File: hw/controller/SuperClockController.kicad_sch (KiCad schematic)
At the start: 64 parts, among them J1 USB_A, J2 ATmega ISP, J3 Led Cathodes, J4 Led Anodes, J5 Yellow LED 0, J6 Yellow LED 1, Q1 IRLML2502, Q10 IRLML2502, Q11 IRLML2502, Q12 IRLML2502, Q13 IRLML2502, Q14 IRLML2502, Q15 IRLML2502, Q16 IRLML2502, Q17 IRLML2502, Q18 IRLML2502, Q2 IRLML2502, Q3 IRLML2502, Q4 IRLML2502, Q5 IRLML2502, Q6 IRLML2502, Q7 IRLML2502, Q8 IRLML2502, Q9 IRLML2502, SW1 SW_Push, SW2 SW_Push, SW3 SW_Push, U1 ATmega32A-A, U2 DS3231SN, U3 DS1307ZN, Y1 16MHz, Y2 32.768kHz

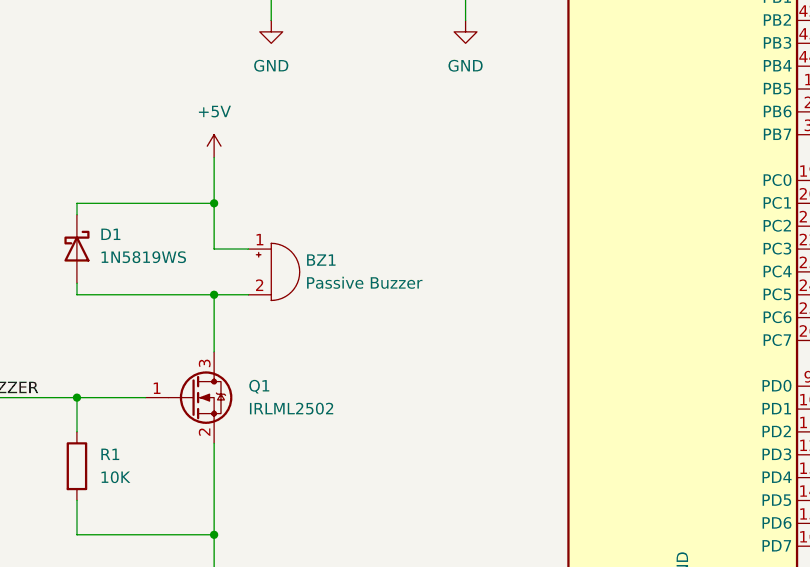
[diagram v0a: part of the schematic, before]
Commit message: Mention buzzer resistance on schematic
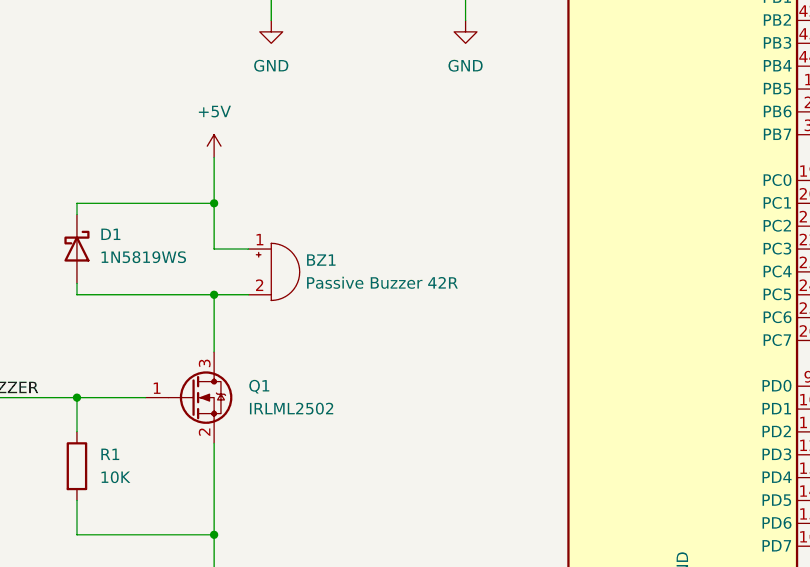
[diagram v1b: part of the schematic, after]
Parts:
- BZ1: value Passive Buzzer -> Passive Buzzer 42R
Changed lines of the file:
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@@
 			)
 		)
-		(property "Value" "Passive Buzzer"
+		(property "Value" "Passive Buzzer 42R"
 			(at 62.23 152.3999 0)
 			(effects

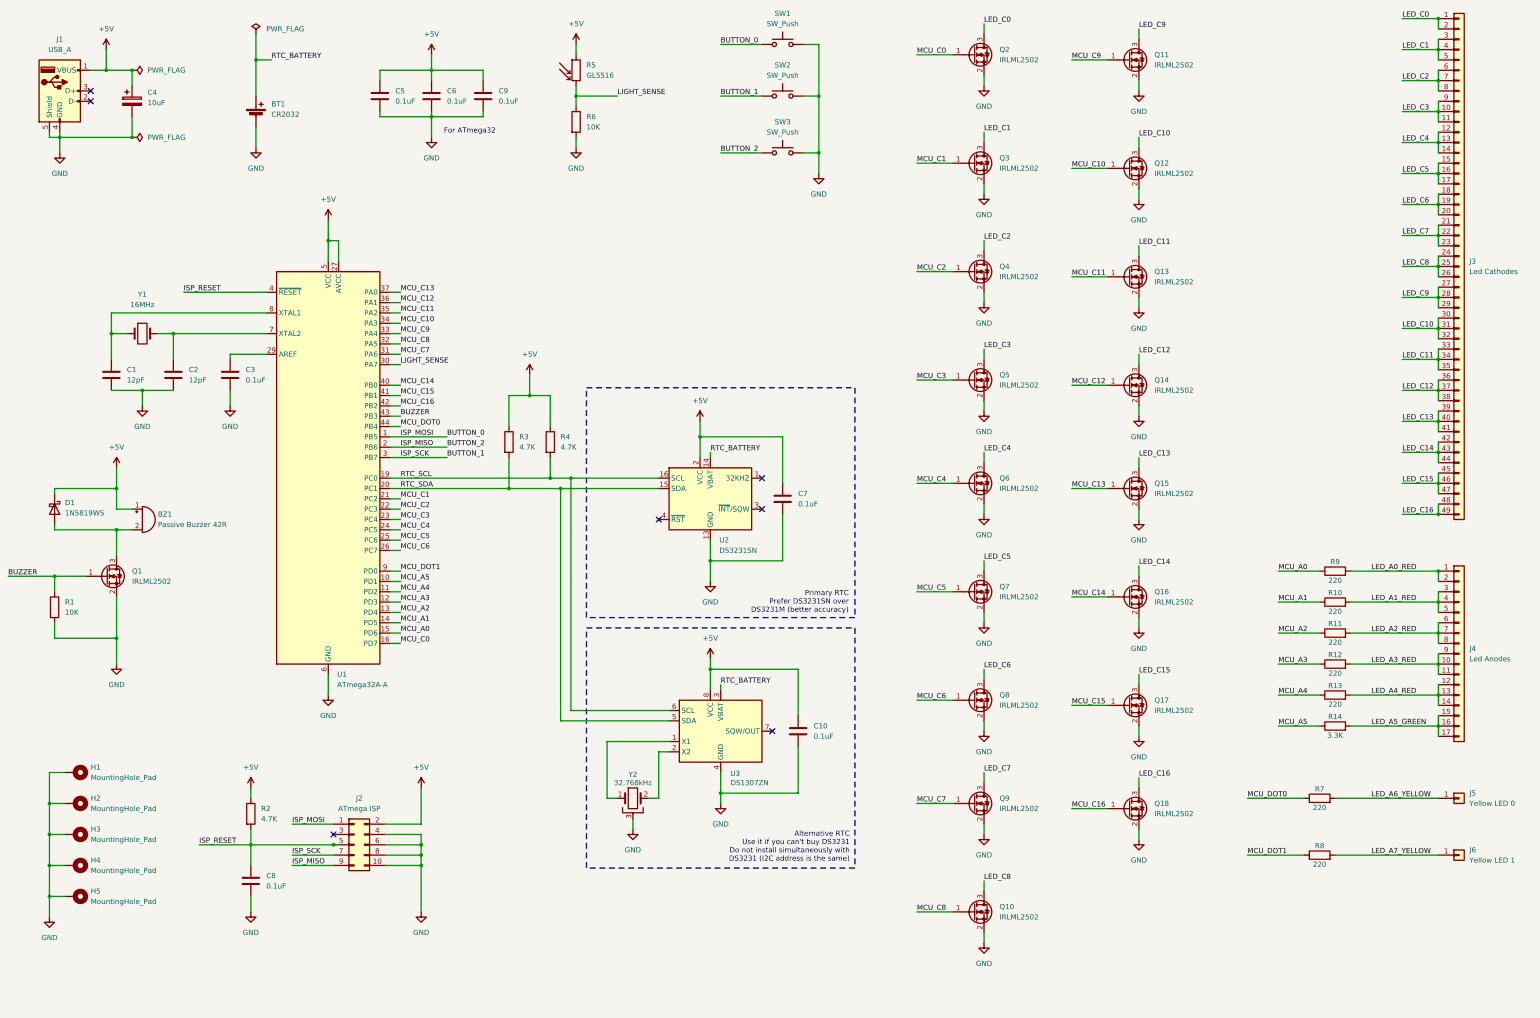
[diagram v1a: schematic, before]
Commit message: Controller PCB revision 3.1
- Add cathode pull-ups. It seems to be the only proper way to deal with ghosting and flickering on lowest brightness
- Connect all anodes to one MCU port, should provide more opportunities to software.
- Use smaller silk-screen outline for CR2032 holder (the previous one was visibly offset for my battery holder).
- Update component numbering with a more sensible scheme: cathode FETs and resistors are now numbers 1-17.
- Use bigger footprint and bigger value for power input capacitor.
- Add missing capacitor to one of MCU power pins.
- Move crystal closer to MCU.
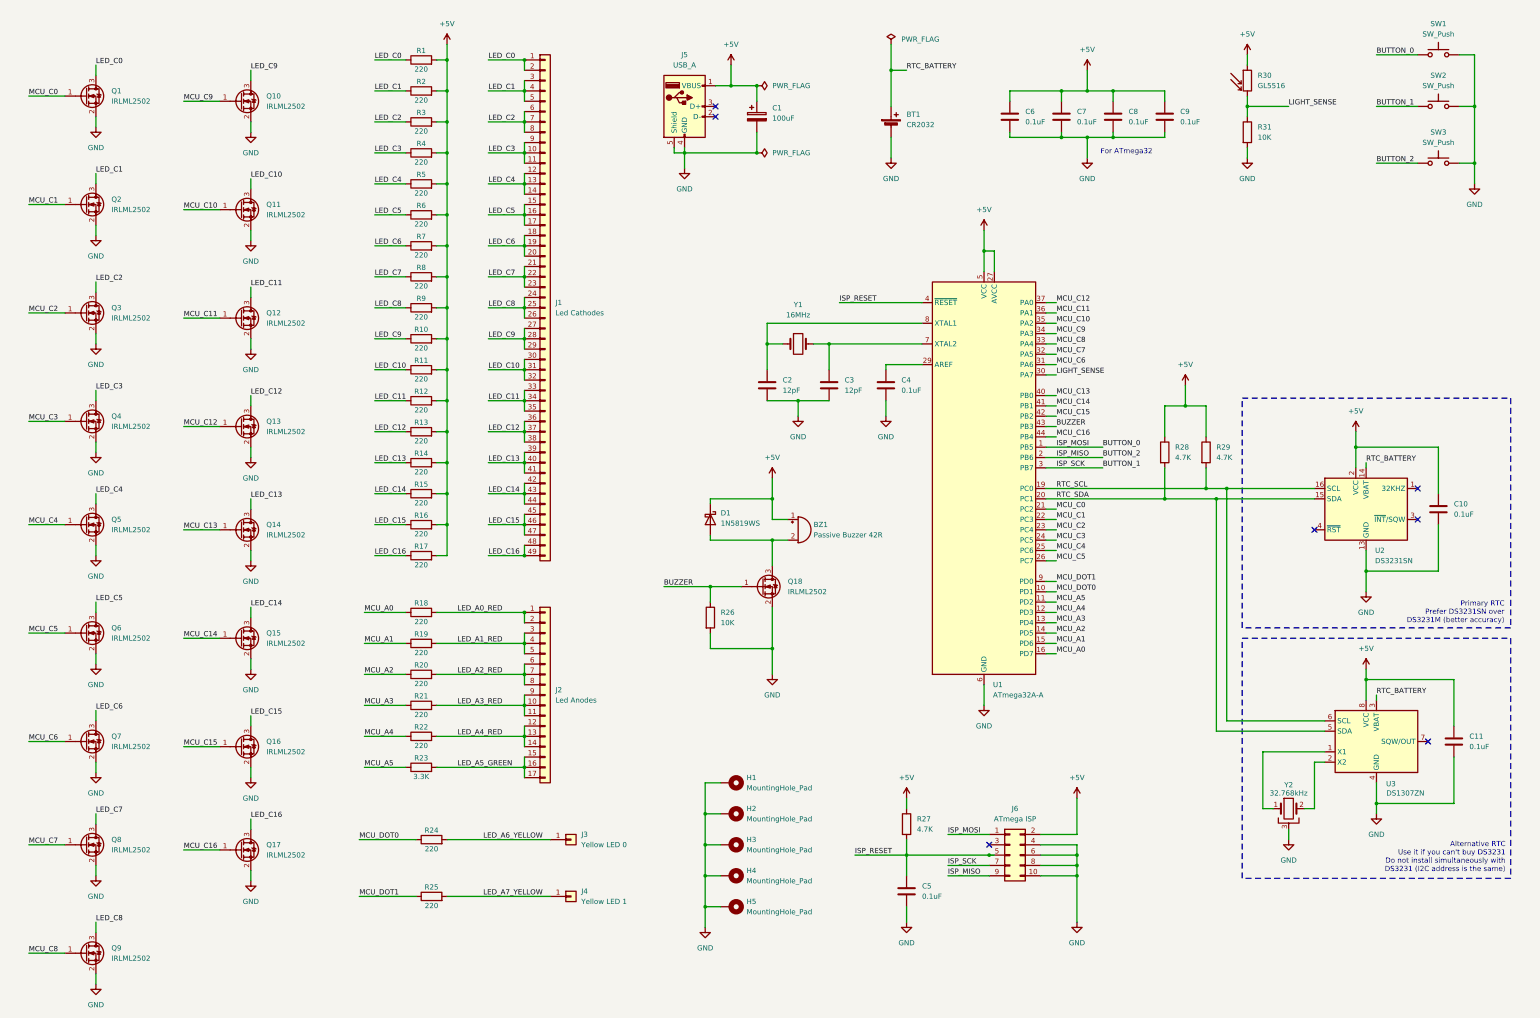
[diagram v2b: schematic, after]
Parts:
- added C9: 0.1uF, Capacitor_SMD:C_0805_2012Metric_Pad1.18x1.45mm_HandSolder, symbol Device:C
- added R1, R10, R11, R12, R13, R14, R15, R16, R17, R2, R3, R4, R5, R6, R7, R8, R9: 220, Resistor_SMD:R_0805_2012Metric_Pad1.20x1.40mm_HandSolder, symbol Device:R
- BT1: footprint Battery:Battery_Panasonic_CR2032-HFN_Horizontal_CircularHoles -> @Project:Battery_CR2032
- BZ1: footprint @Project:Buzzer_12x7.5RM6.5 -> @Project:Buzzer_12x8.5
- C1: renamed from C4; value 10uF -> 100uF; footprint Capacitor_Tantalum_SMD:CP_EIA-6032-28_Kemet-C_Pad2.25x2.35mm_HandSolder -> Capacitor_Tantalum_SMD:CP_EIA-7343-31_Kemet-D_Pad2.25x2.55mm_HandSolder
- renumbered C7 to C10, C10 to C11, C1 to C2, C2 to C3, C3 to C4, C8 to C5, C5 to C6, C6 to C7, C9 to C8, J3 to J1, J4 to J2, J5 to J3, J6 to J4, J1 to J5, J2 to J6, Q2 to Q1, Q11 to Q10, Q12 to Q11, Q13 to Q12, Q14 to Q13, Q15 to Q14, Q16 to Q15, Q17 to Q16, Q18 to Q17, Q1 to Q18, Q3 to Q2, Q4 to Q3, Q5 to Q4, Q6 to Q5, Q7 to Q6, Q8 to Q7, Q9 to Q8, Q10 to Q9, R9 to R18, R10 to R19, R11 to R20, R12 to R21, R13 to R22, R14 to R23, R7 to R24, R8 to R25, R1 to R26, R2 to R27, R3 to R28, R4 to R29, R5 to R30, R6 to R31
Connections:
- net +5V: now also C9.1, R1.2, R10.2, R11.2, R12.2, R13.2, R14.2, R15.2, R16.2, R17.2, R2.2, R3.2, R4.2, R5.2, R6.2, R7.2, R8.2, R9.2
- net GND: now also C9.2
- net LED_C0: now also R1.1
- net LED_C1: now also R2.1
- net LED_C10: now also R11.1
- net LED_C11: now also R12.1
- net LED_C12: now also R13.1
- net LED_C13: now also R14.1
- net LED_C14: now also R15.1
- net LED_C15: now also R16.1
- net LED_C16: now also R17.1
- net LED_C2: now also R3.1
- net LED_C3: now also R4.1
- net LED_C4: now also R5.1
- net LED_C5: now also R6.1
- net LED_C6: now also R7.1
- net LED_C7: now also R8.1
- net LED_C8: now also R9.1
- net LED_C9: now also R10.1
- net MCU_A0: now also U1.16 (PD7); no longer U1.15 (PD6)
- net MCU_A1: now also U1.15 (PD6); no longer U1.14 (PD5)
- net MCU_A2: now also U1.14 (PD5); no longer U1.13 (PD4)
- net MCU_A3: now also U1.13 (PD4); no longer U1.12 (PD3)
- net MCU_A4: now also U1.12 (PD3); no longer U1.11 (PD2)
- net MCU_A5: now also U1.11 (PD2); no longer U1.10 (PD1)
- net MCU_C0: now also U1.21 (PC2); no longer U1.16 (PD7)
- net MCU_C1: now also U1.22 (PC3); no longer U1.21 (PC2)
- net MCU_C10: now also U1.35 (PA2); no longer U1.34 (PA3)
- net MCU_C11: now also U1.36 (PA1); no longer U1.35 (PA2)
- net MCU_C12: now also U1.37 (PA0); no longer U1.36 (PA1)
- net MCU_C13: now also U1.40 (PB0); no longer U1.37 (PA0)
- net MCU_C14: now also U1.41 (PB1); no longer U1.40 (PB0)
- net MCU_C15: now also U1.42 (PB2); no longer U1.41 (PB1)
- net MCU_C16: now also U1.44 (PB4); no longer U1.42 (PB2)
- net MCU_C2: now also U1.23 (PC4); no longer U1.22 (PC3)
- net MCU_C3: now also U1.24 (PC5); no longer U1.23 (PC4)
- net MCU_C4: now also U1.25 (PC6); no longer U1.24 (PC5)
- net MCU_C5: now also U1.26 (PC7); no longer U1.25 (PC6)
- net MCU_C6: now also U1.31 (PA6); no longer U1.26 (PC7)
- net MCU_C7: now also U1.32 (PA5); no longer U1.31 (PA6)
- net MCU_C8: now also U1.33 (PA4); no longer U1.32 (PA5)
- net MCU_C9: now also U1.34 (PA3); no longer U1.33 (PA4)
- net MCU_DOT0: now also U1.10 (PD1); no longer U1.44 (PB4)
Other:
- title: SuperClock v3 Controller -> SuperClock v3.1 Controller
- moved on the sheet: BT1, BZ1, C1, C10, C11, C2, C3, C4, C5, C6, C7, C8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
